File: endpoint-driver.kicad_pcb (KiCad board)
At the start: 2 copper layers, 40 x 40 mm, 37 parts, among them J1 Conn_01x04, J2 Conn_01x04_Pin, J3 Conn_01x04_Pin, J4 Conn_01x02_Pin, J5 Conn_01x03_Pin, J6 Conn_01x03_Pin, J7 Conn_01x03_Pin, J8 Conn_01x04, U1 JW5017S, U2 STM32G431CBUx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

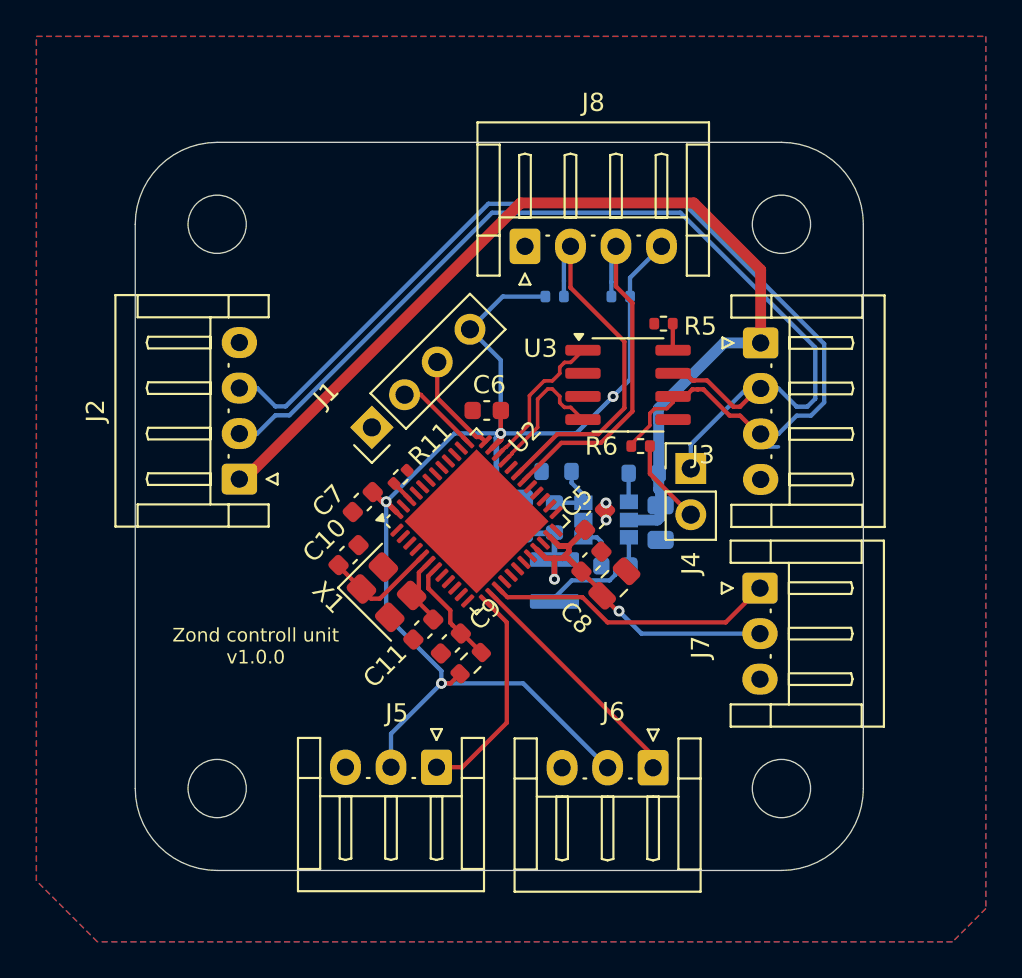
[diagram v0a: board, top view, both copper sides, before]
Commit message: Refactor PCB design parameters in endpoint-driver - Adjusted minimum hole-to-hole clearance from 0.25 to 0.24 in the .kicad_pro file for improved spacing.
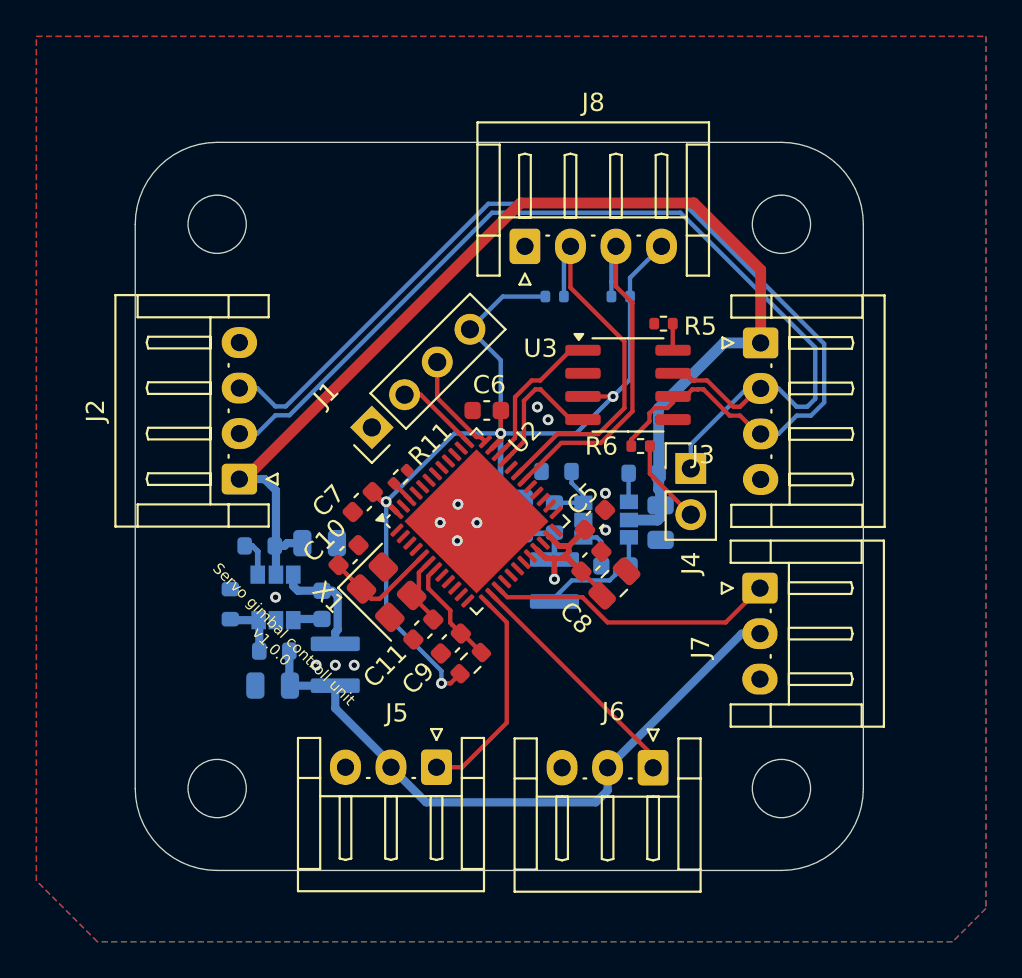
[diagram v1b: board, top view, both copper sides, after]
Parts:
- added C12: 100nF, Capacitor_SMD:C_0603_1608Metric, B.Cu at (10.3, -14.6)
- added C13: 4.7uF, Capacitor_SMD:C_0805_2012Metric, B.Cu at (10.1, -18.0)
- added C14: 10uF, Capacitor_SMD:C_0805_2012Metric, B.Cu at (7.55, -10.2)
- added L2: 4.7uH, my_lib:SNR3015K-4R7M, B.Cu at (11.0, -11.3)
- added R10: 100kOm, PCM_Resistor_SMD_AKL:R_0603_1608Metric, B.Cu at (6.84, -17.8)
- added R12: 3kOm, PCM_Resistor_SMD_AKL:R_0603_1608Metric, B.Cu at (5.22, -14.6)
- added R9: 16kOm, PCM_Resistor_SMD_AKL:R_0603_1608Metric, B.Cu at (7.64, -12.1)
- added U4: JW5017S, my_lib:JW5017S, B.Cu at (7.73, -15.0)
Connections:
- J5 pad 2: +3.3V -> +5V
- J6 pad 2: +3.3V -> +5V
- J7 pad 2: +3.3V -> +5V
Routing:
- net +5V: track 0.00 -> 35.8 mm
- net +3.3V: track 98.9 -> 74.0 mm, vias 6 -> 5
- net VCC: track 55.4 -> 64.0 mm
- net Net-(U4-SW): track 0.00 -> 6.03 mm
- net Net-(U4-FB): track 0.00 -> 3.30 mm
- net Net-(U4-EN): track 0.00 -> 2.12 mm
- net Net-(U4-BST): track 0.00 -> 1.61 mm
- net /CAN/CAN_N: track 58.9 -> 57.7 mm
- net /CAN/CAN_OUT-: track 8.48 -> 7.97 mm
- net GND: vias 2 -> 12
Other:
- board text added: "Servo gimbal controll unit v1.0.0"
- board text removed: "Zond controll unit v1.0.0"
